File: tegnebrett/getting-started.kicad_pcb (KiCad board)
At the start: 2 copper layers, 1 part

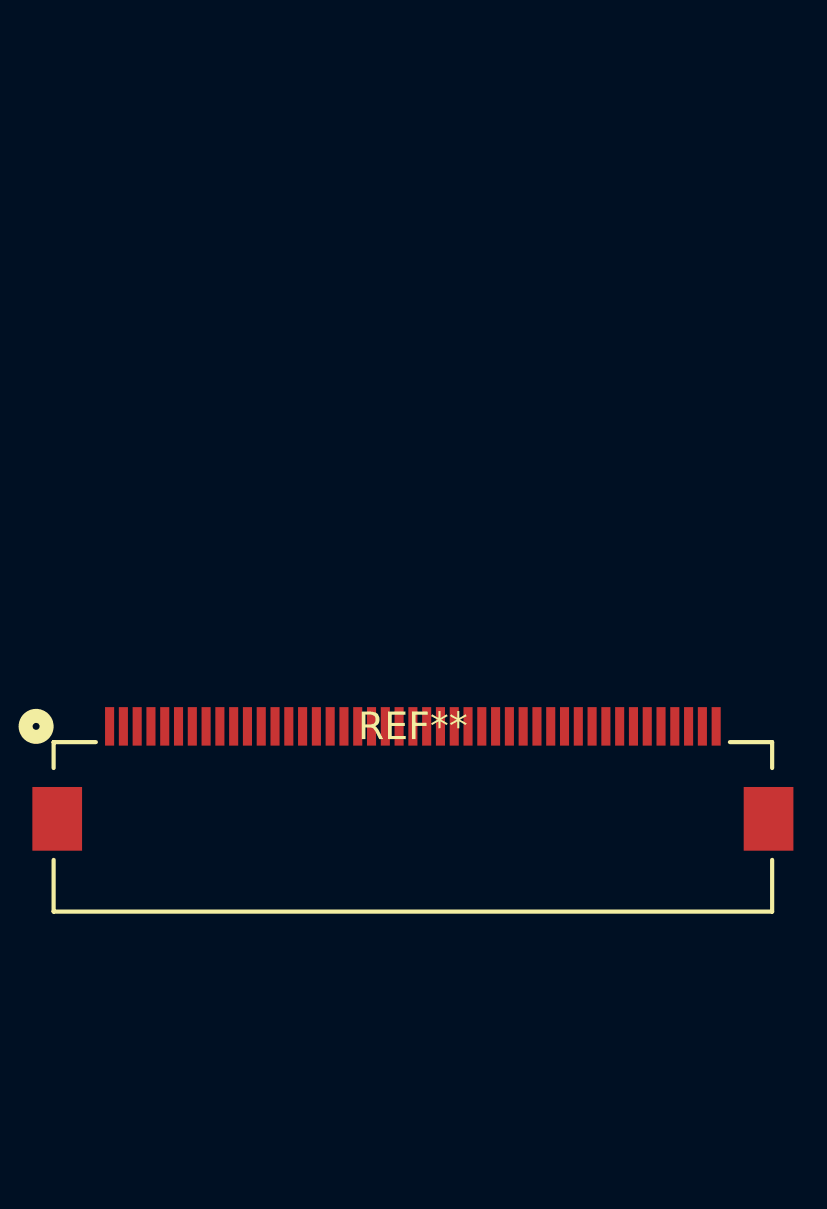
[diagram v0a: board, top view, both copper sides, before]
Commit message: feat: add USB-A symbol and footprint to schematic
Also included the 3D model. Now there's some stuff in the PCB.
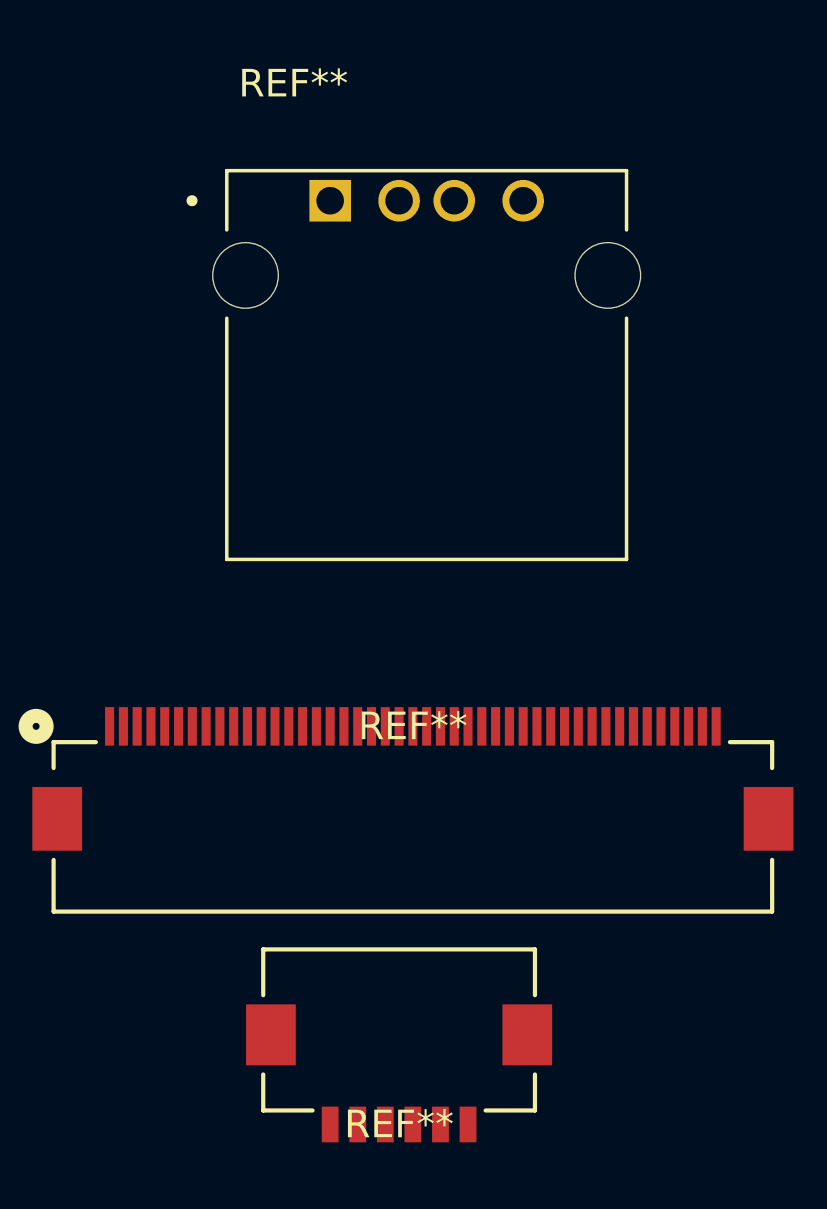
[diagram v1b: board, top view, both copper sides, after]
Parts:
- added REF**: CON6_1X6_DRBF_HST_HIR, tegnebrett_modules:CON6_1X6_DRBF_HST_HIR, F.Cu at (119.0, 112.0)
- added REF**: OST_USB-A1HSW6, tegnebrett_modules:OST_USB-A1HSW6, F.Cu at (120.0, 84.0)

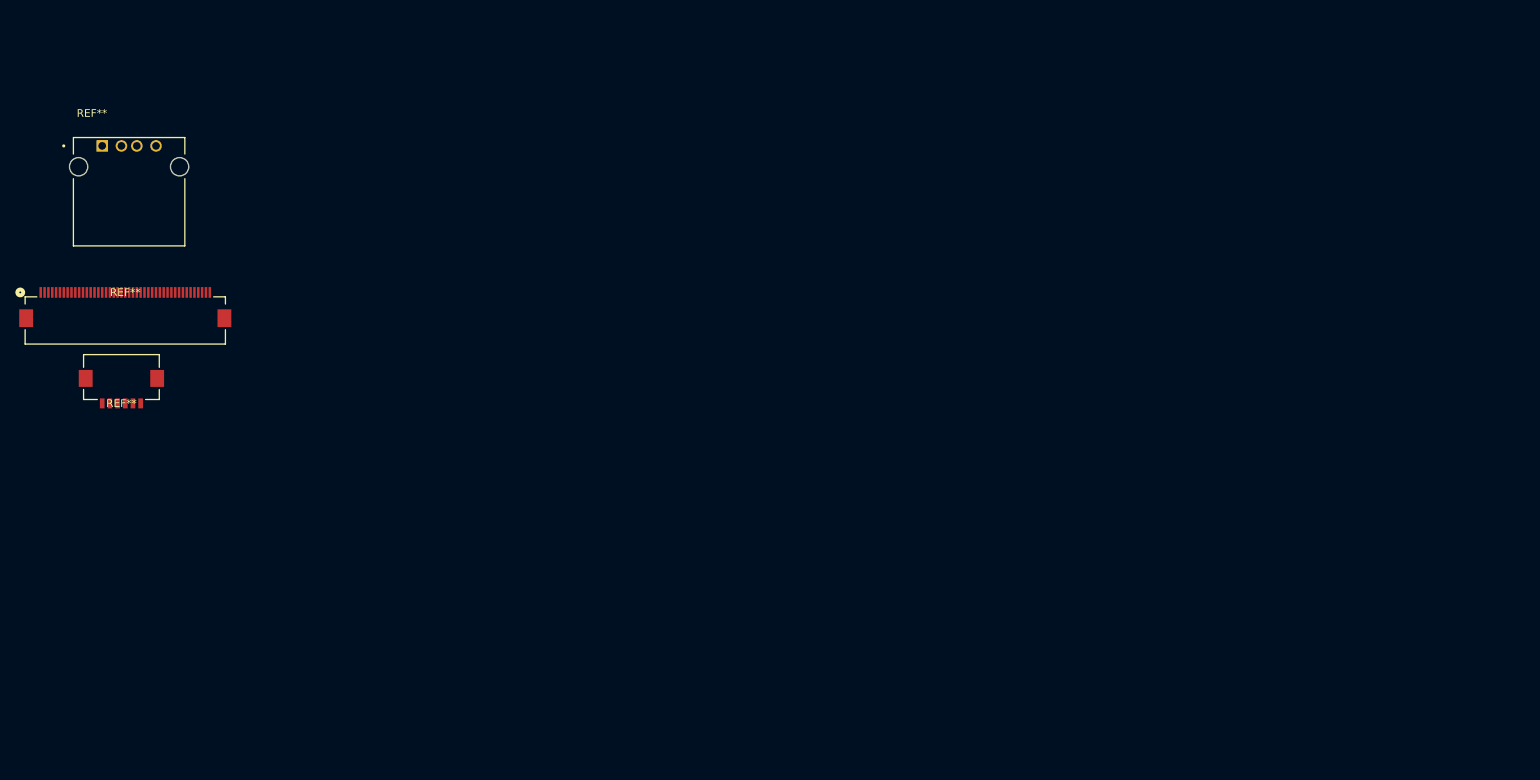
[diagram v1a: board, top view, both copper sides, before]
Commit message: feat: add 3d-models to custom footprints
6pin and 45pin, USB-A.
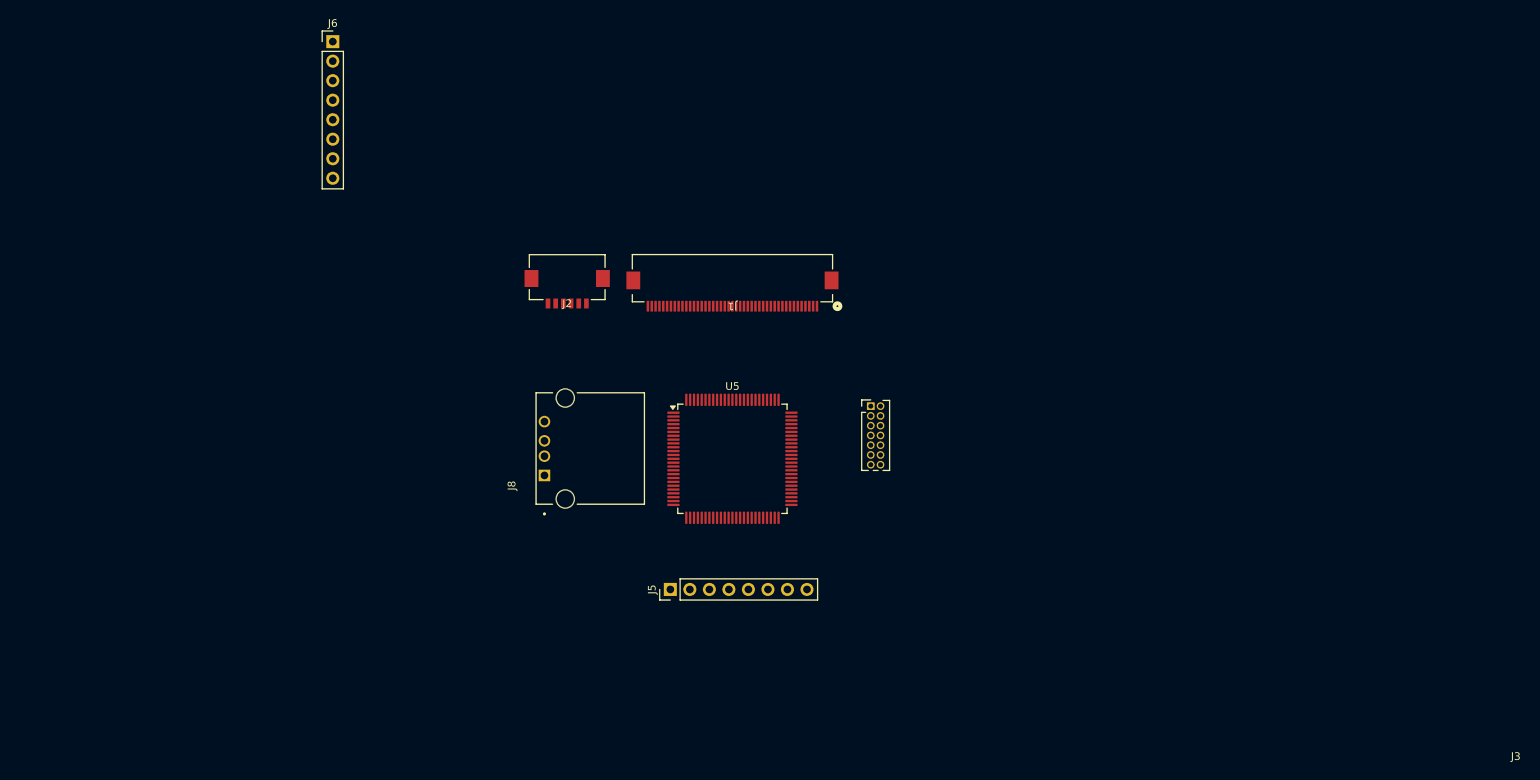
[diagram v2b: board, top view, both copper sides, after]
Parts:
- removed REF**: CON6_1X6_DRBF_HST_HIR, tegnebrett_modules:CON6_1X6_DRBF_HST_HIR
- removed REF**: OST_USB-A1HSW6, tegnebrett_modules:OST_USB-A1HSW6
- removed REF**: CONN_45S-0.5SH55, tegnebrett_modules:CONN_45S-0.5SH55
- added J1: FH12-45S-0.5SH55, tegnebrett_modules:CONN_45S-0.5SH55, F.Cu at (198.5, 98.5)
- added J2: FH12-6S-1SH55, tegnebrett_modules:CON6_1X6_DRBF_HST_HIR, F.Cu at (177.0, 99.0)
- added J3: Conn_ST_STDC14, Connector_PinHeader_1.27mm:PinHeader_2x07_P1.27mm_Vertical, F.Cu at (216.5, 115.2)
- added J5: MCU_Header_Pin, Connector_PinHeader_2.54mm:PinHeader_1x08_P2.54mm_Vertical, F.Cu at (190.4, 139.0)
- added J6: FPGA_Header_Pin, Connector_PinHeader_2.54mm:PinHeader_1x08_P2.54mm_Vertical, F.Cu at (146.5, 67.7)
- added J8: USB-A1HSW6, tegnebrett_modules:OST_USB-A1HSW6, F.Cu at (176.8, 120.7)
- added U5: STM32U5G7VJTxQ, Package_QFP:LQFP-100_14x14mm_P0.5mm, F.Cu at (198.5, 122.0)

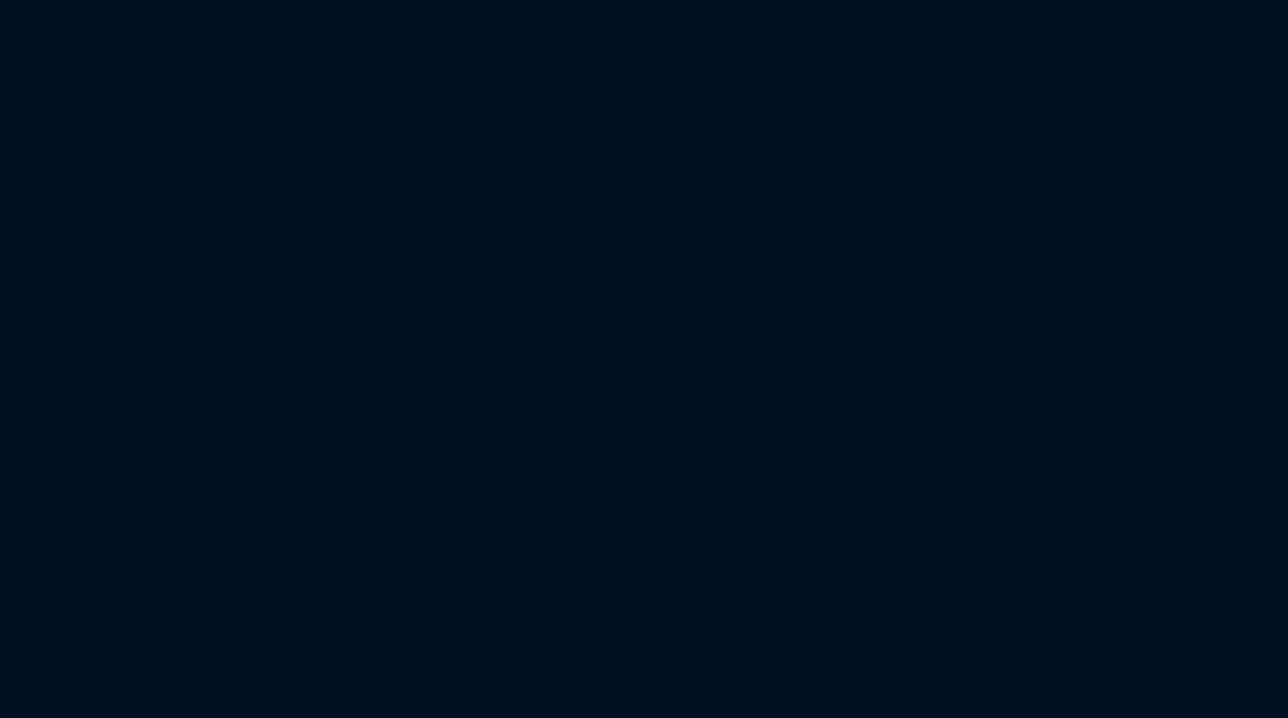
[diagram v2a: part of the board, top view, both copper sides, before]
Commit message: feat: Add footprint to VGA
Also add VGA to PCB layout.
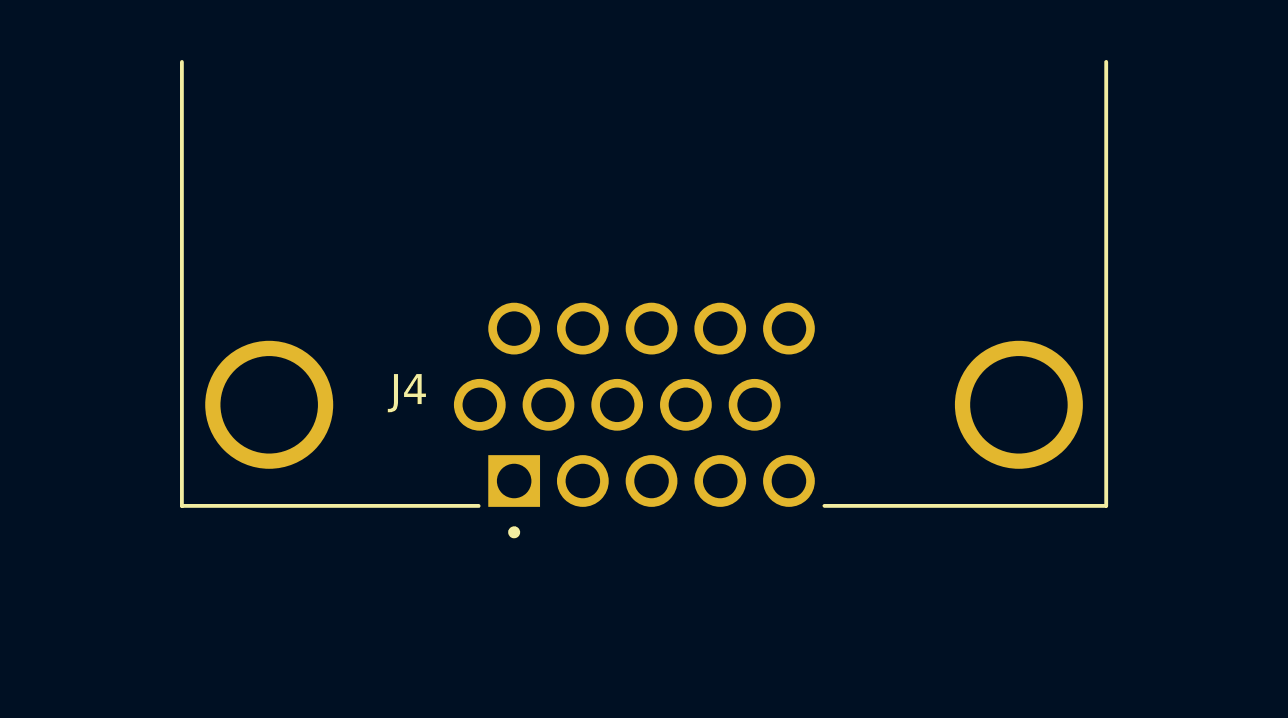
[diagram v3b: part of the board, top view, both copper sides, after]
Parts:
- added J4: DA15_Socket, tegnebrett_modules:AMPHENOL_L77HDE15SD1CH4RHNVGA, F.Cu at (265.7, 29.5)
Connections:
- J3 pad 10: /DEBUG_JTDI -> Net-(J3-JTDI/NC)
- J3 pad 4: /DEBUG_SWDIO -> Net-(J3-JTMS/SWDIO)
- J3 pad 6: /DEBUG_SWCLK -> Net-(J3-JCLK/SWCLK)
- J3 pad 8: /DEBUG_SWO -> Net-(J3-JTDO/SWO)

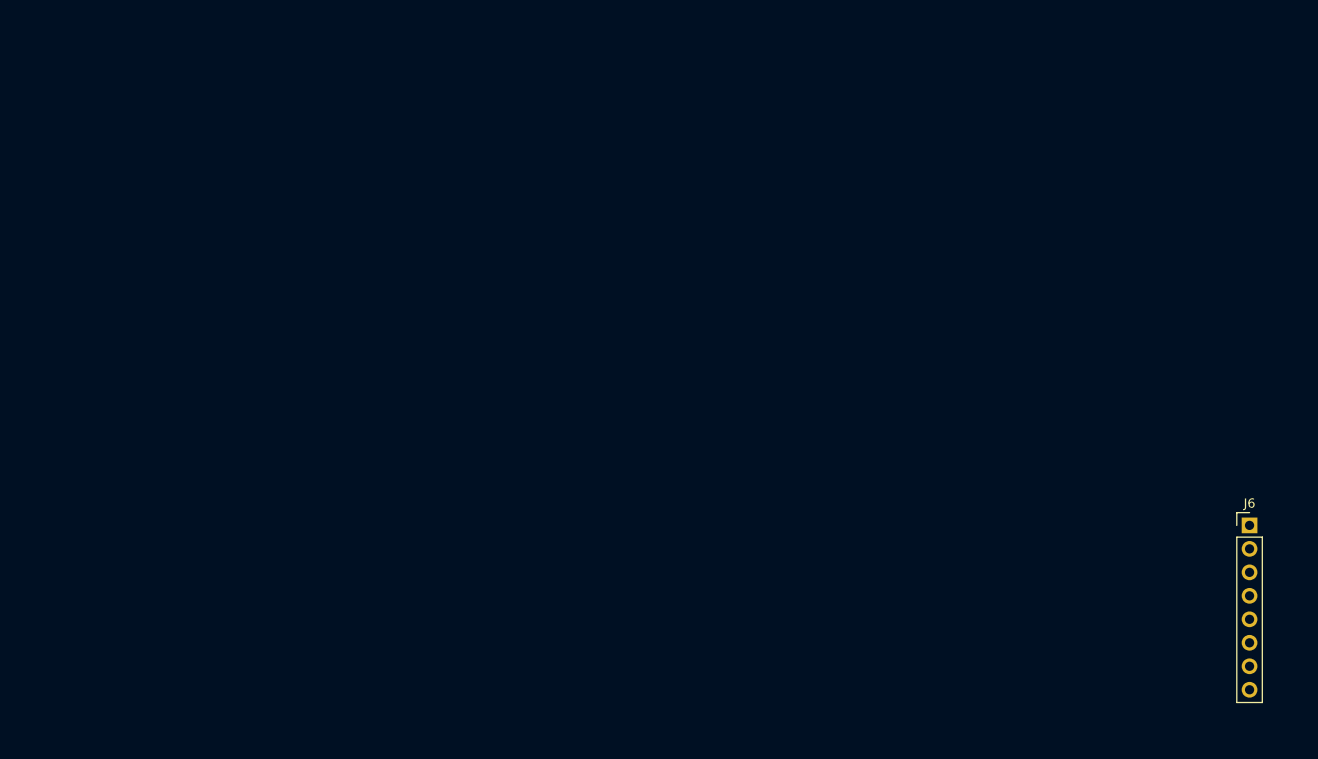
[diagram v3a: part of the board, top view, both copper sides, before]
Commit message: feat: add 100MHz oscillator footprint
Additionally add the footprint to PCB.
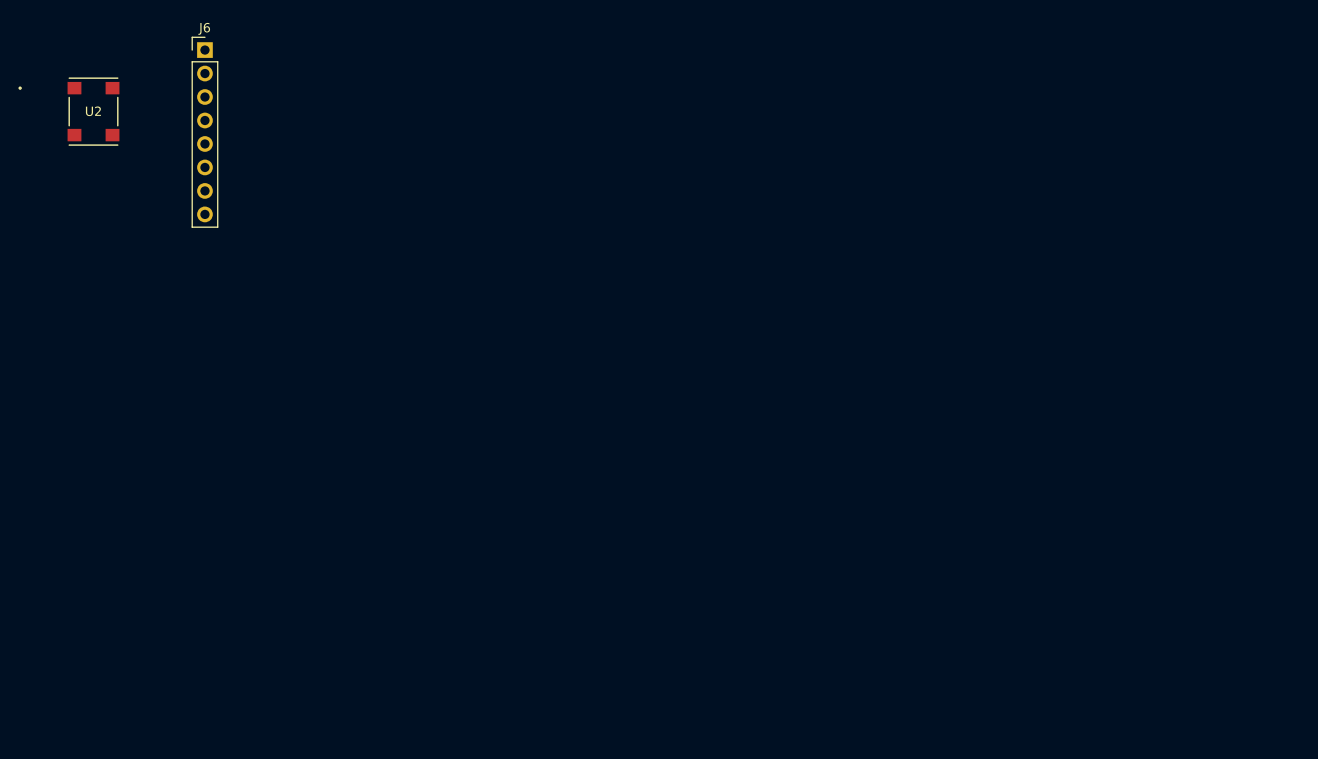
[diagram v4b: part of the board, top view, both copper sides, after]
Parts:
- added U2: Oscillator 100MHz, tegnebrett_modules:CWX813-100.0M_CNW, F.Cu at (21.4, 23.0)
- moved J6 124.1 mm to (33.5, 16.3)

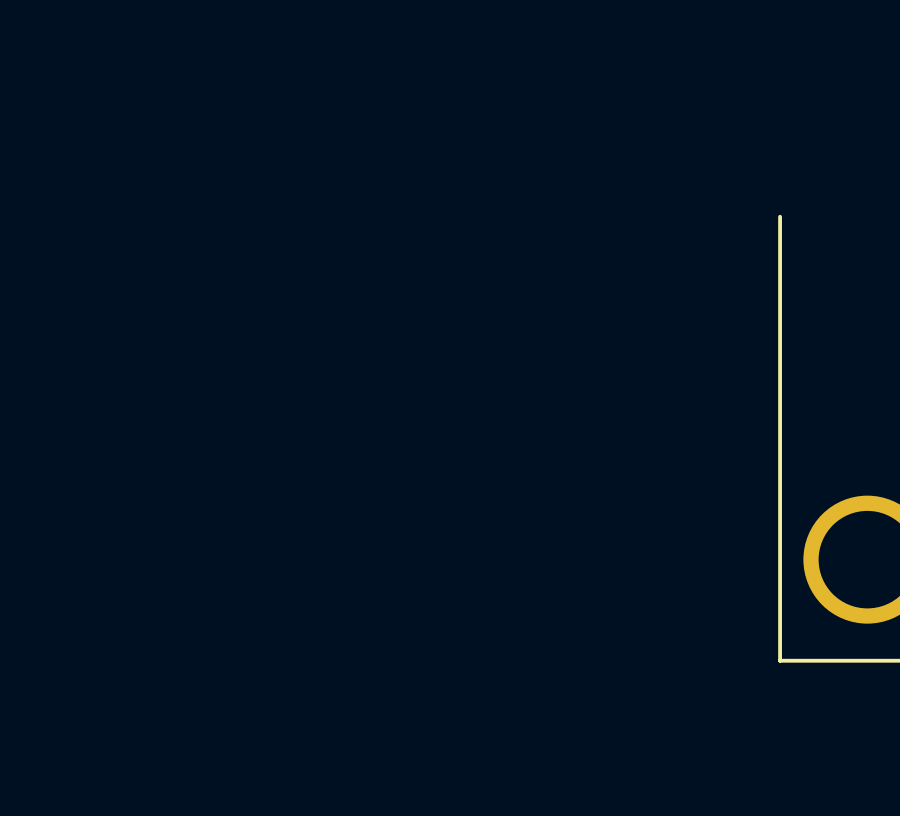
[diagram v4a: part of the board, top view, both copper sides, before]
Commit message: feat: add VGA Transceiver footprint
Additionally add VGA Transceiver to PCB layout.
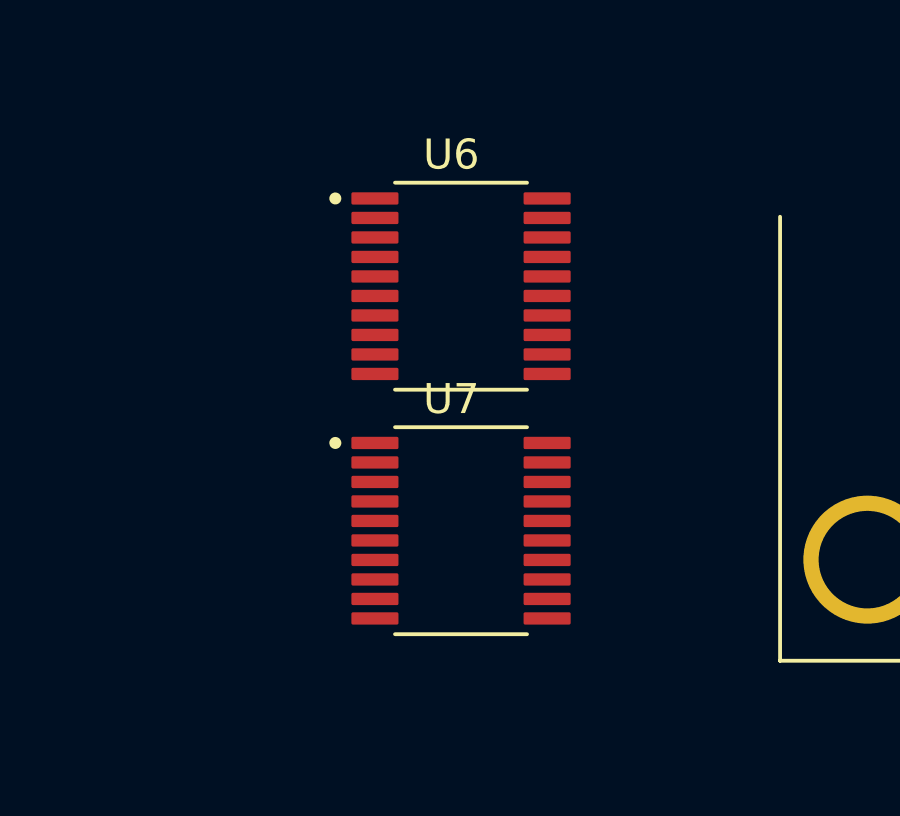
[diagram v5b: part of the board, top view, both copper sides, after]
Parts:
- added U6: VGA Transceiver, tegnebrett_modules:SOP65P640X120-20N, F.Cu at (239.6, 20.4)
- added U7: VGA Transciever, tegnebrett_modules:SOP65P640X120-20N, F.Cu at (239.6, 28.6)
